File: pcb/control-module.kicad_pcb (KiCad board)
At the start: 2 copper layers, 136.9 x 69.9 mm, 168 parts, among them J1 Screw_Terminal_01x06, J3 USB_C_Receptacle_USB2.0_16P, J4 Micro_SD_Card, J5 Conn_ST_STDC14, J6 Conn_Coaxial, J7 Conn_ST_STDC14, Q1 SiS454DN, Q2 SiS454DN, SW1 SW_DIP_x04, SW2 SW_DIP_x04, U1 TPS2116DRL, U10 MIC5504-3.3YM5, U2 USBLC6-2SC6, U3 STM32U545RETxQ, U4 MS5607-02BA, U5 LSM6DSL, U6 MCP73831-2-OT, U7 MIC5504-3.3YM5, U8 SAM-M10Q-00B, U9 STM32WL55CCUx, Y1 Crystal, Y2 Crystal_GND23

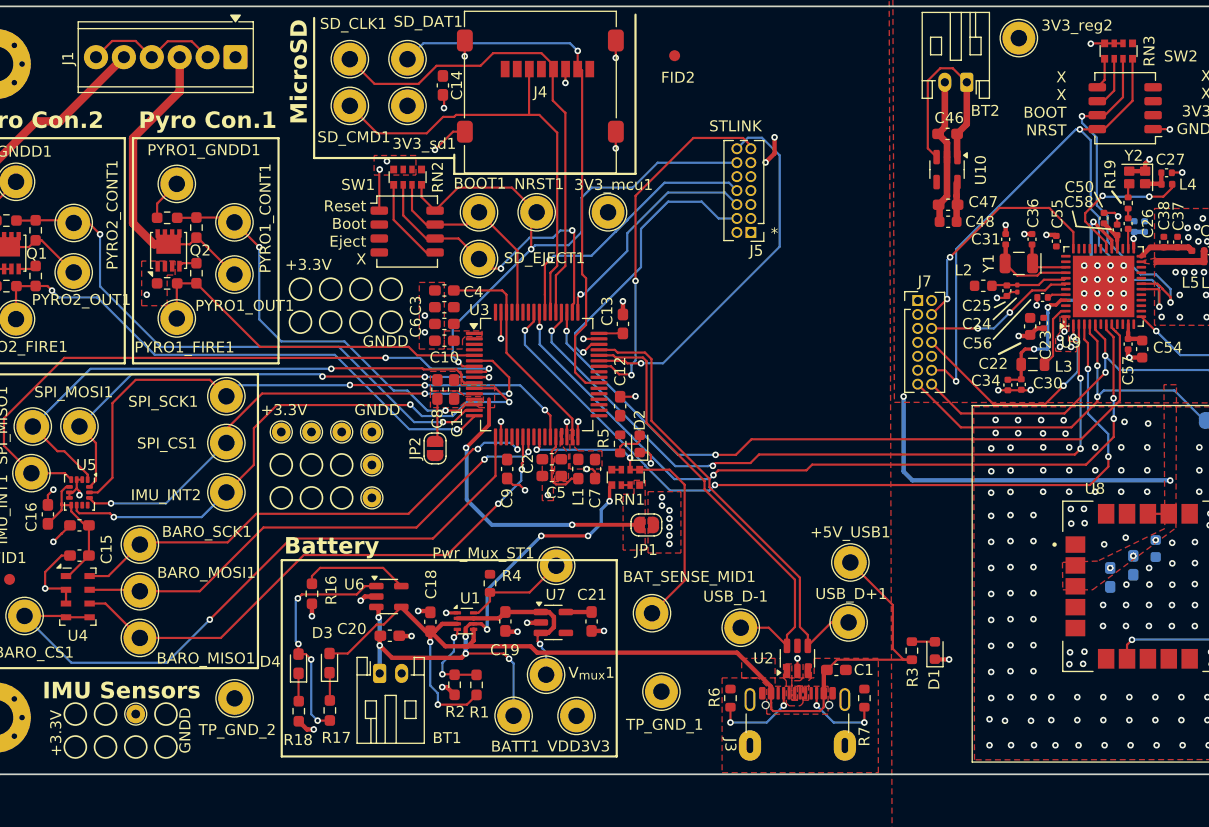
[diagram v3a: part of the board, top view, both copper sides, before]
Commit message: Fabricated version 3_9_26
This version of the board was sent to fabricate on 3/9/26
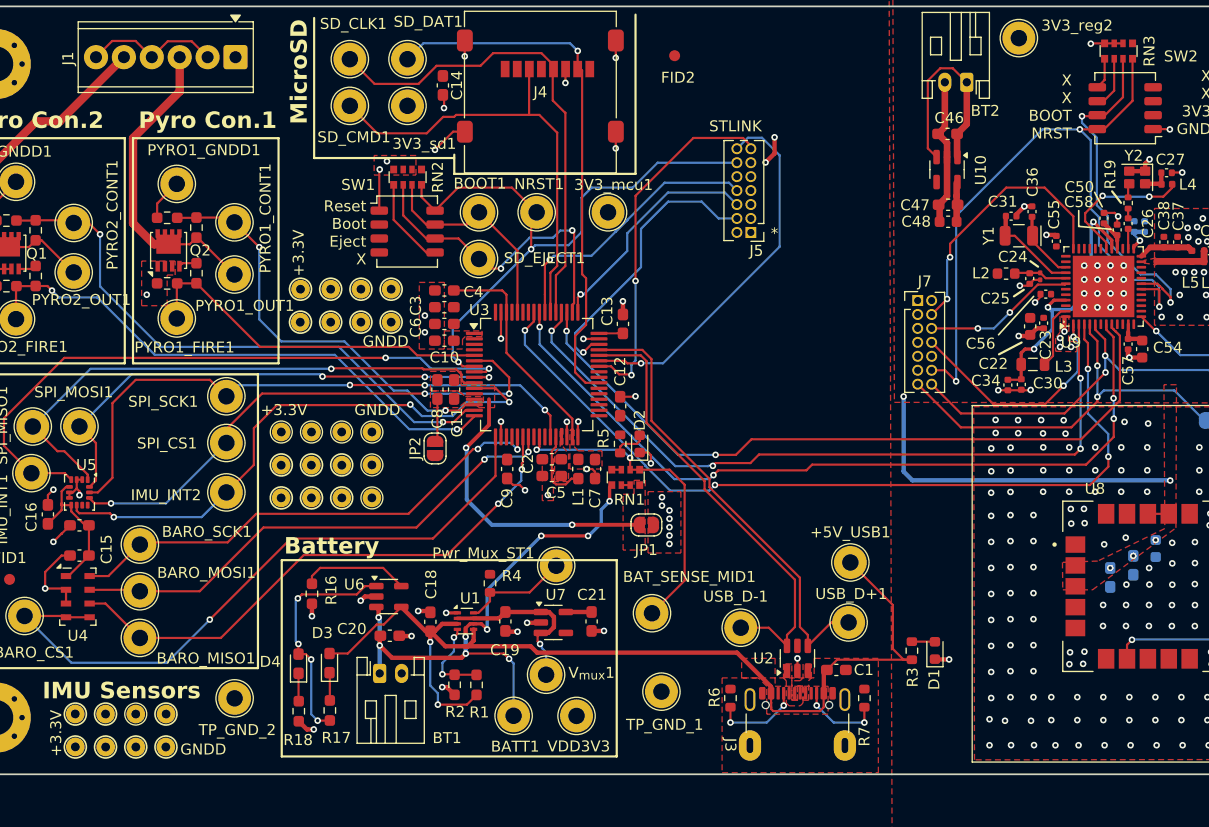
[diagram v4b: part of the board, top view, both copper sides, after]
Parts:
- added ?: , , F.Cu at (156.5, 45.8)
- added ?: , , F.Cu at (127.8, 87.4)
- added ?: , , F.Cu at (153.8, 48.8)
- added ?: , , F.Cu at (146.5, 64.8)
- added ?: , , F.Cu at (152.0, 64.8)
- added ?: , , F.Cu at (152.0, 61.8)
- added ?: , , F.Cu at (130.5, 87.4)
- added ?: , , F.Cu at (149.2, 64.8)
- added ?: , , F.Cu at (148.2, 45.8)
- added ?: , , F.Cu at (151.0, 48.8)
- added ?: , , F.Cu at (130.5, 84.4)
- added ?: , , F.Cu at (149.2, 61.8)
- added ?: , , F.Cu at (133.3, 87.4)
- added ?: , , F.Cu at (148.2, 48.8)
- added ?: , , F.Cu at (156.5, 48.8)
- added ?: , , F.Cu at (153.8, 45.8)
- added ?: , , F.Cu at (151.0, 45.8)
- added ?: , , F.Cu at (136.0, 87.4)
- added ?: , , F.Cu at (146.5, 61.8)
- added ?: , , F.Cu at (127.7, 84.4)
- added ?: , , F.Cu at (136.0, 84.4)
- moved Y1 2.52 mm to (213.7, 40.9)
- moved C36 2.52 mm to (214.8, 38.7)
- moved C24 2.36 mm to (215.6, 44.6)
- moved L2 2.36 mm to (212.5, 44.3)
- moved C25 2.36 mm to (214.6, 44.8)
- moved C31 2.16 mm to (212.9, 39.1), turned to 180 degrees
- moved C56 0.42 mm to (216.1, 46.2)
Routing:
- net /SWDIO_radio: track 21.6 -> 24.6 mm
- net Net-(U9-VDDA): track 6.91 -> 4.78 mm
- net /NRST_radio: track 63.7 -> 65.5 mm
- net +3.3V_radio: track 47.5 -> 46.2 mm
- net Net-(U9-PC14): track 4.84 -> 6.18 mm
- net Net-(U9-PC15): track 7.83 -> 8.59 mm
- net GNDD: track 113.8 -> 114.5 mm, vias 345 -> 344
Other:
- board text added: "{dblquote}Computah, launch this rocket{dblquote}"
